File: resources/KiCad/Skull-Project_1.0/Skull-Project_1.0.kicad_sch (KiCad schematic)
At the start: 7 parts, among them SW1 SW_SPST, SW2 SW_SPST

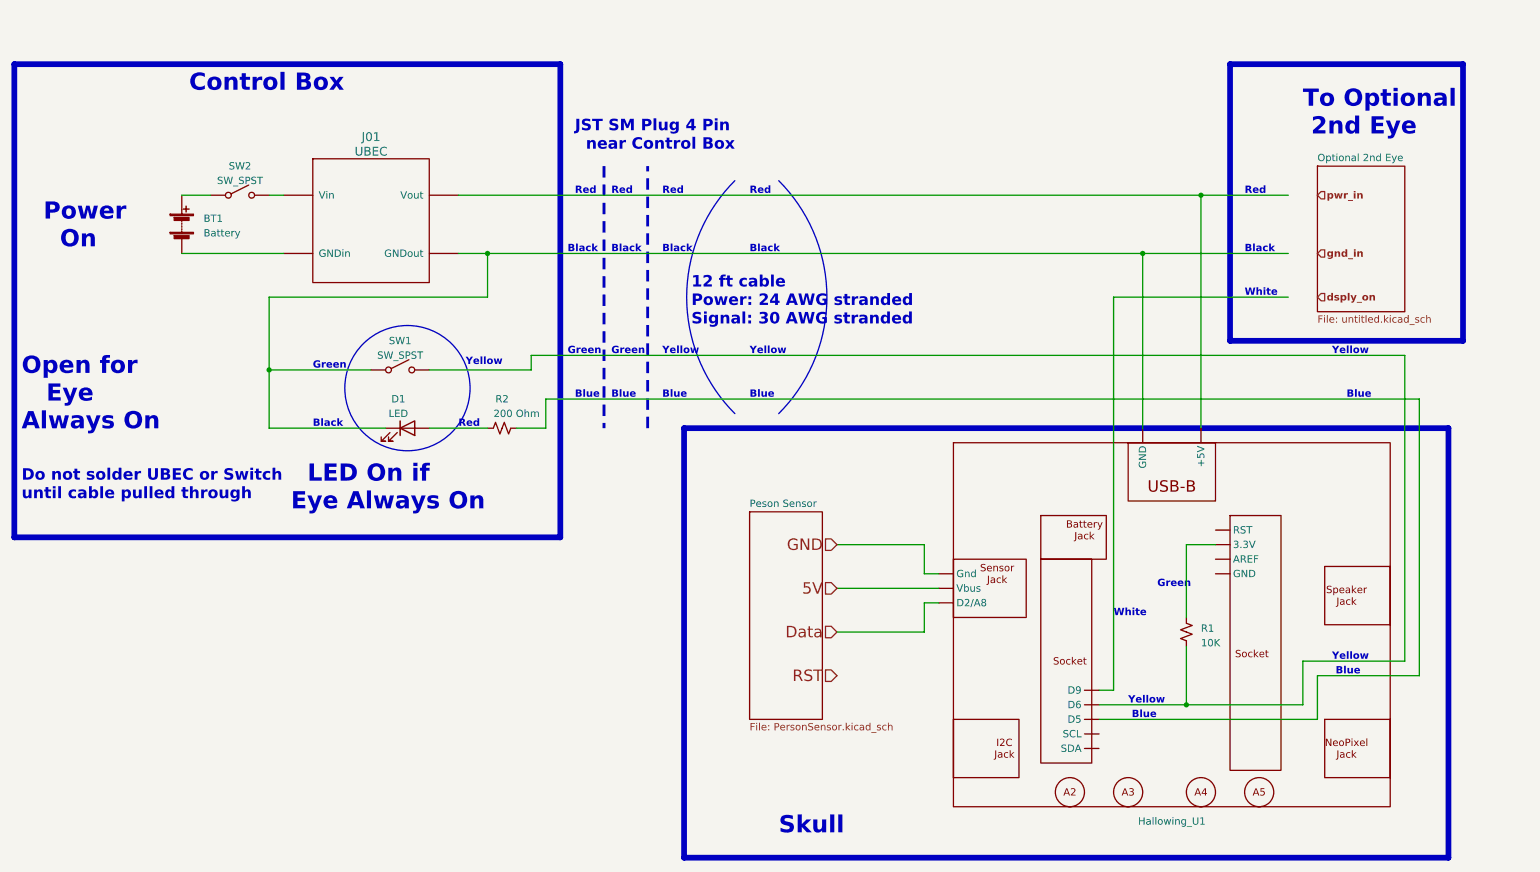
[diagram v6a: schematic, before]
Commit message: clean up schematic
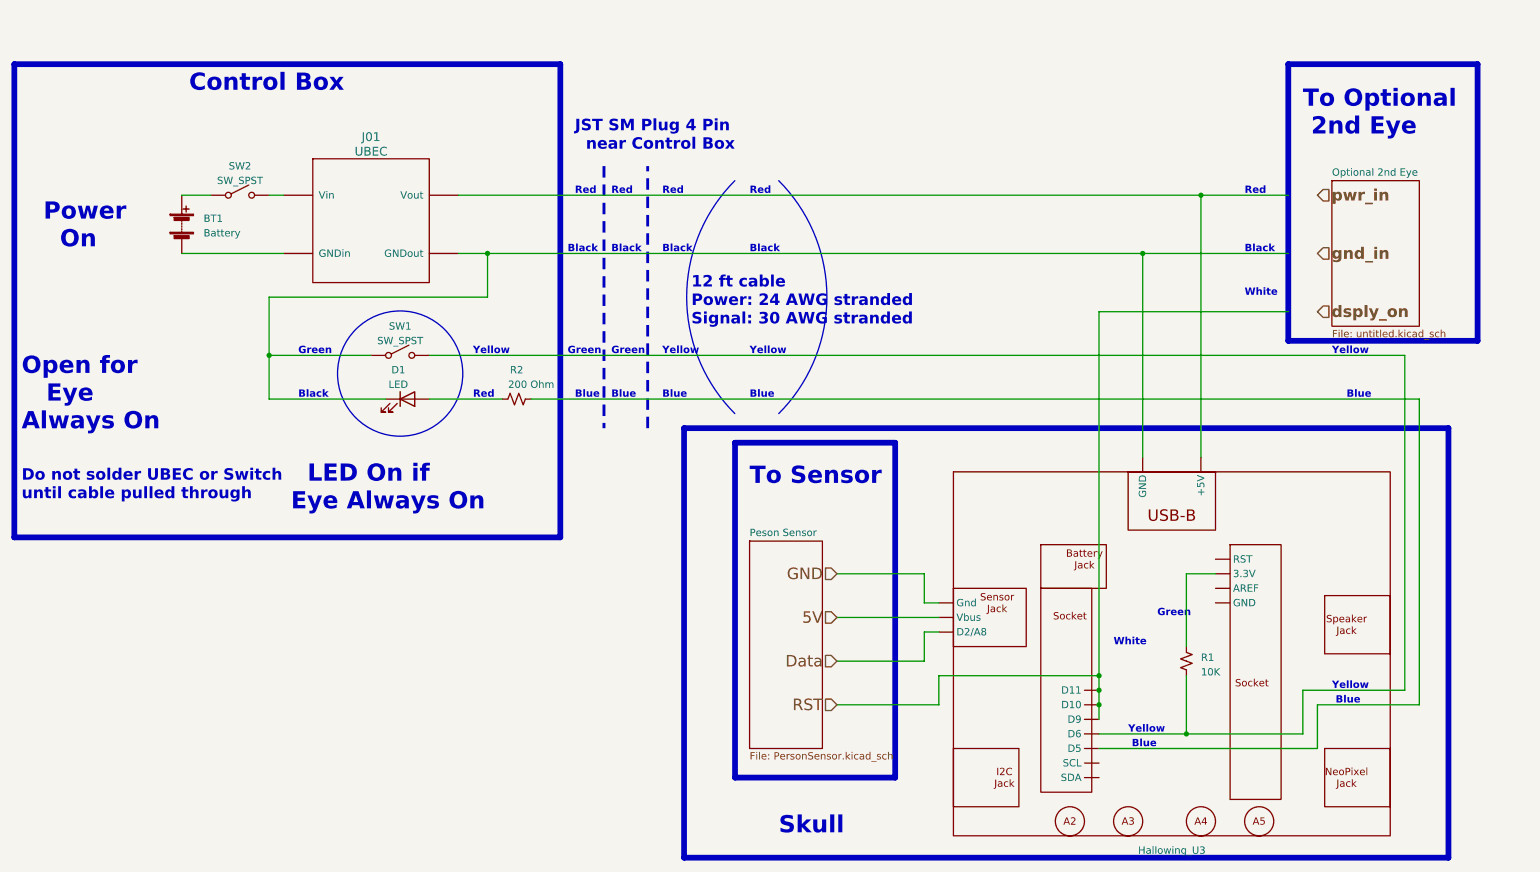
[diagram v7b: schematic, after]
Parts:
- removed Hallowing_U1: ~, symbol mdoLibrary:Hallowing_M4
- added Hallowing_U3: ~, symbol mdoLibrary:Hallowing_M4
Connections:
- net at R2.2: now also Hallowing_U3. (Vbus)
- net at SW2.~ (B): now also BT1.1 (+)
- net at R1.1: now also Hallowing_U3. (Vbus)
- net at R1.2, SW1.~ (B): now also Hallowing_U3. (Vbus)
- net at D1.1 (K), SW1.~ (B): now also Hallowing_U3. (Vbus)
- new net 5V : Hallowing_U3. (Vbus)
- new net Data : Hallowing_U3. (Vbus)
- new net GND : Hallowing_U3. (Vbus)
- new net RST : Hallowing_U3. (Vbus)
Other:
- note added: "To Sensor"
- moved on the sheet: D1, R1, R2, SW1

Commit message: microwave sensor now uses NANO for edge detect
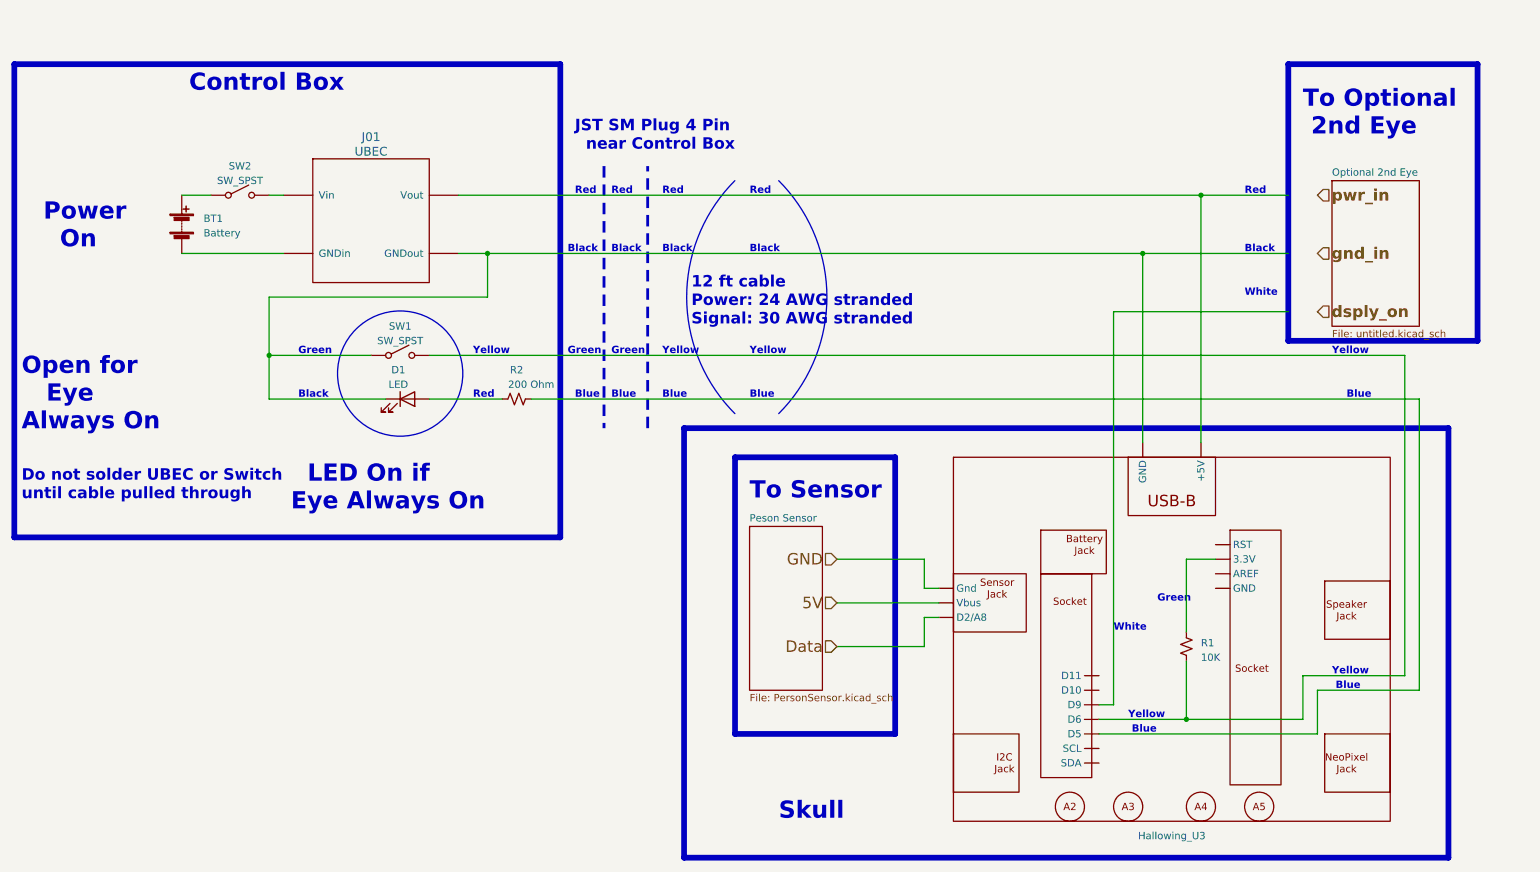
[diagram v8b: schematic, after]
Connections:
- net RST  is gone; now on net GND : Hallowing_U3. (Vbus)
- net at SW2.~ (B): now also BT1.1 (+)
- new net: Hallowing_U3. (Vbus), R1.2, SW1.~ (B)
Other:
- moved on the sheet: Hallowing_U3, R1
